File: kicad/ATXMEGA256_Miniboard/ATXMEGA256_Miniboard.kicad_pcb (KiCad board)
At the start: 4 copper layers, 50 x 70 mm, 42 parts, among them J1 1x2 Screw Terminal, J10 2x5 Goldpin Socket, J11 2x5 Goldpin Socket, J12 2x3 Goldpin Socket, J13 2x5 Goldpin Socket, J14 2x5 Goldpin Socket, J2 10118192-0001LF, J3 2x5 IDC Socket, J4 2x3 Goldpin Socket, J5 2x3 Goldpin Header, J6 1x2 Goldpin Header, J7 1x2 Goldpin Header, J8 1x3 Goldpin Header, J9 2x5 Goldpin Socket, Q1 MMFTP3334K, SW1 RESET, U1 ATXMEGA256A3B-AU, U2 MCP1703A-3302E/DB, Y1 32.768 kHz, Y2 16 MHz

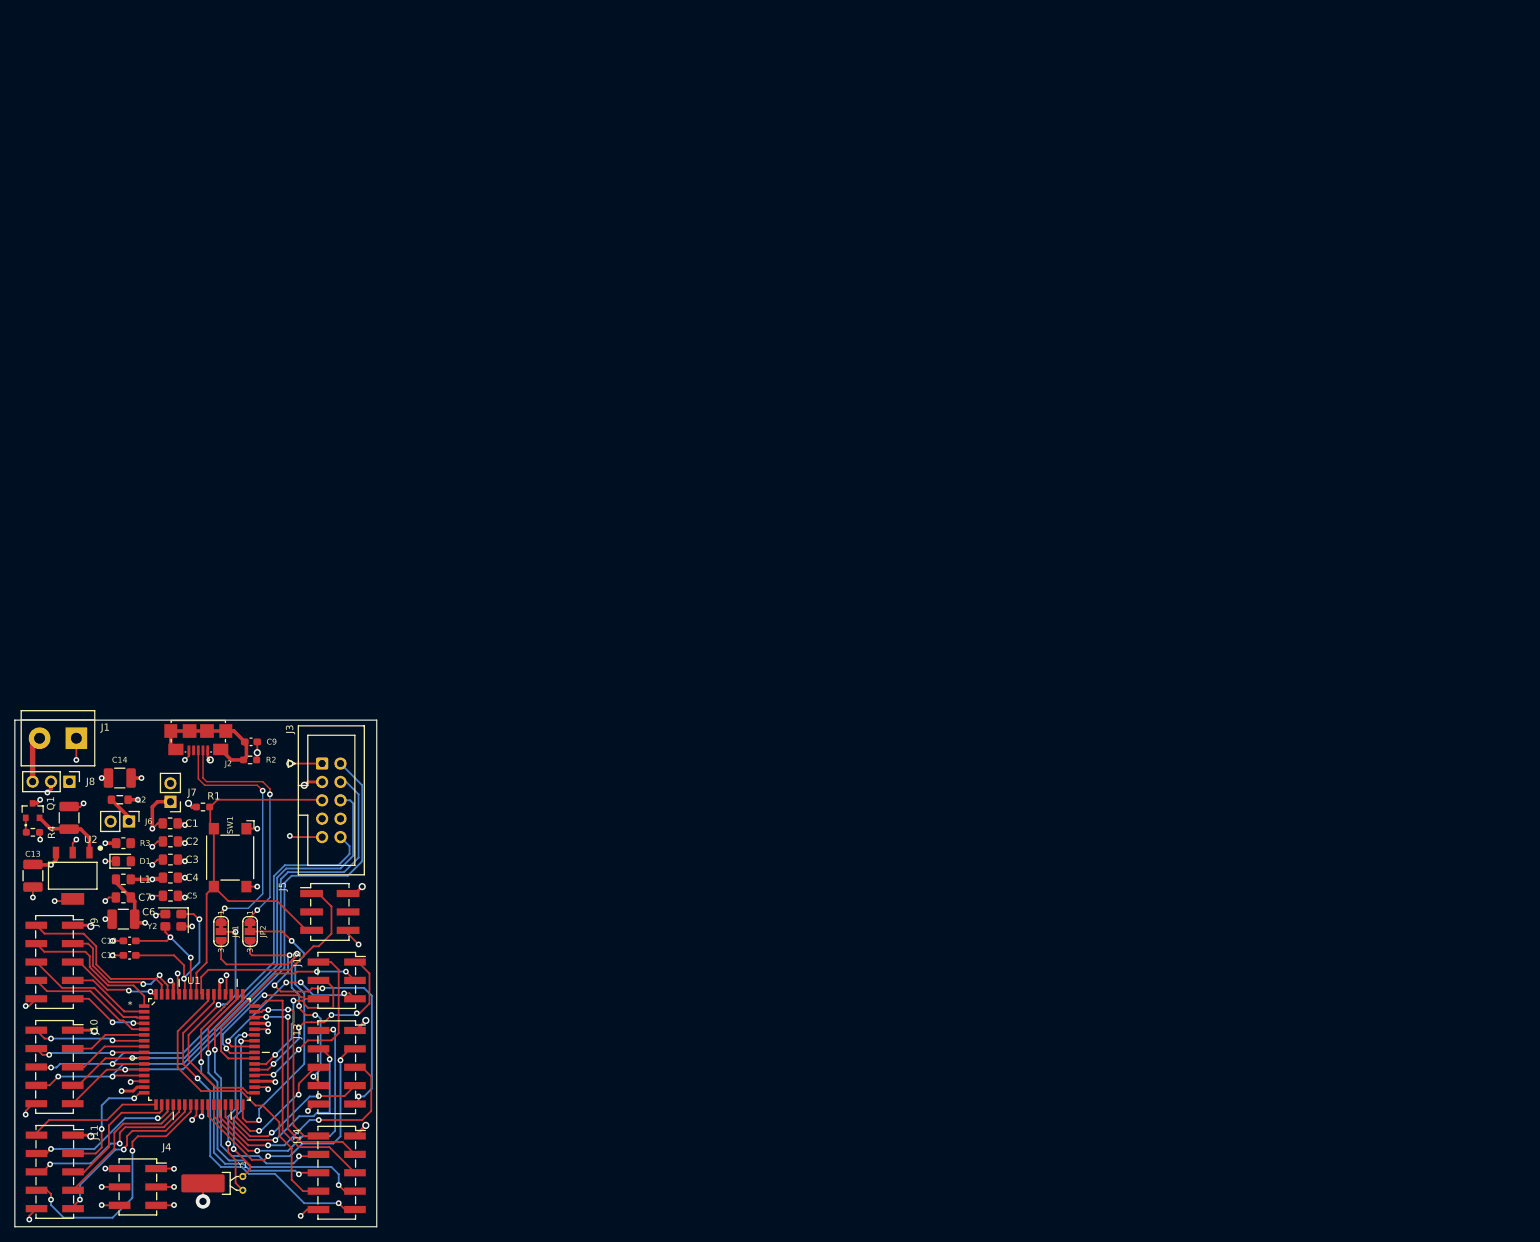
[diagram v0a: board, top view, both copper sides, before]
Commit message: layout komponentów
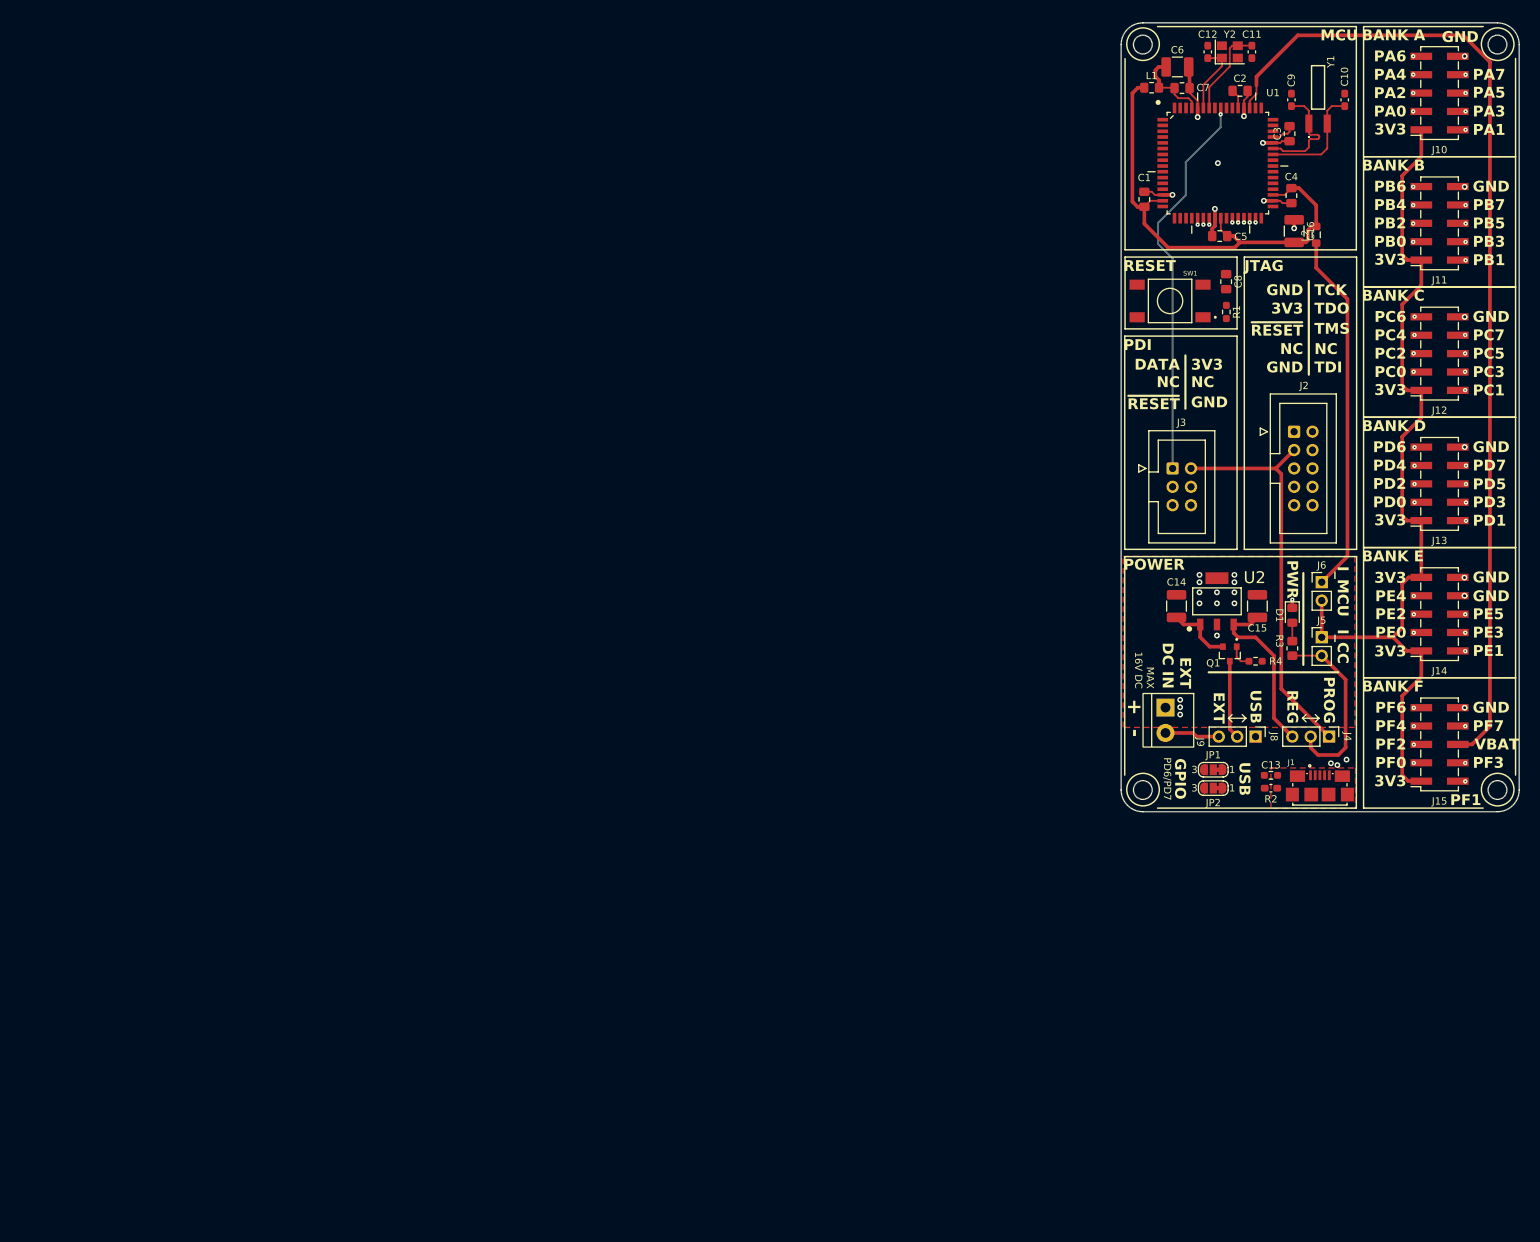
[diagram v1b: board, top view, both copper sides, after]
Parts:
- removed J7: 1x2 Goldpin Header, Connector_PinHeader_2.54mm:PinHeader_1x02_P2.54mm_Vertical
- added C15: 10u, Capacitor_SMD:C_1210_3225Metric_Pad1.33x2.70mm_HandSolder, F.Cu at (186.7, 110.7)
- added C16: 10u, Capacitor_SMD:C_1210_3225Metric_Pad1.33x2.70mm_HandSolder, F.Cu at (191.8, 58.9)
- added C8: 100n, Capacitor_SMD:C_0805_2012Metric_Pad1.18x1.45mm_HandSolder, F.Cu at (182.4, 65.9)
- added G***: LOGO, logo:onyx_logo, B.Cu at (316.2, 90.7)
- added J15: 2x5 Goldpin Socket, Connector_PinSocket_2.54mm:PinSocket_2x05_P2.54mm_Vertical_SMD, F.Cu at (211.9, 129.9)
- added REF**: KiCad-Logo2_6mm_SilkScreen, Symbol:KiCad-Logo2_6mm_SilkScreen, B.Cu at (350.3, 92.8)
- added REF**: ESD-Logo_6.6x6mm_SilkScreen, Symbol:ESD-Logo_6.6x6mm_SilkScreen, B.Cu at (334.0, 120.8)
- added REF**: OSHW-Logo2_14.6x12mm_SilkScreen, Symbol:OSHW-Logo2_14.6x12mm_SilkScreen, B.Cu at (375.4, 90.0)
- C10: value 12p -> 22p
- C12: value 10u -> 12p; footprint Capacitor_SMD:C_1210_3225Metric_Pad1.33x2.70mm_HandSolder -> Capacitor_SMD:C_0603_1608Metric_Pad1.08x0.95mm_HandSolder
- C13: value 10u -> 4n7; footprint Capacitor_SMD:C_1210_3225Metric_Pad1.33x2.70mm_HandSolder -> Capacitor_SMD:C_0603_1608Metric_Pad1.08x0.95mm_HandSolder
- C9: value 4n7 -> 22p
- J1: value 1x2 Screw Terminal -> 10118192-0001LF; footprint TerminalBlock:TerminalBlock_bornier-2_P5.08mm -> 10118192-0001LF:AMPHENOL_10118192-0001LF
- J12: value 2x3 Goldpin Socket -> 2x5 Goldpin Socket; footprint Connector_PinSocket_2.54mm:PinSocket_2x03_P2.54mm_Vertical_SMD -> Connector_PinSocket_2.54mm:PinSocket_2x05_P2.54mm_Vertical_SMD
- J2: value 10118192-0001LF -> 2x5 IDC Socket; footprint 10118192-0001LF:AMPHENOL_10118192-0001LF -> Connector_IDC:IDC-Header_2x05_P2.54mm_Vertical
- J3: value 2x5 IDC Socket -> 2x3 IDC Socket; footprint Connector_IDC:IDC-Header_2x05_P2.54mm_Vertical -> Connector_IDC:IDC-Header_2x03_P2.54mm_Vertical
- J4: value 2x3 Goldpin Socket -> 1x3 Goldpin Header; footprint Connector_PinSocket_2.54mm:PinSocket_2x03_P2.54mm_Vertical_SMD -> Connector_PinHeader_2.54mm:PinHeader_1x03_P2.54mm_Vertical
- J5: value 2x3 Goldpin Header -> 1x2 Goldpin Header; footprint Connector_PinHeader_2.54mm:PinHeader_2x03_P2.54mm_Vertical_SMD -> Connector_PinHeader_2.54mm:PinHeader_1x02_P2.54mm_Vertical
- J9: value 2x5 Goldpin Socket -> 1x2 Screw Terminal; footprint Connector_PinSocket_2.54mm:PinSocket_2x05_P2.54mm_Vertical_SMD -> DG381-3.5-02P-13-00AH:DG381-3.5-02P-13-00AH
- SW1: footprint Button_Switch_SMD:SW_SPST_Omron_B3FS-100xP -> FSM2JSMAA:SW_SMD_2-1437565-8_4_4.50_6.00_6.00_5.00
- Y1: footprint Crystal:Crystal_DS26_D2.0mm_L6.0mm_Horizontal_1EP_style1 -> LFXTAL025159:LFXTAL025159Reel
- moved J10 234.0 mm to (211.9, 39.9), turned to 180 degrees
- moved J11 231.9 mm to (211.9, 57.9), turned to 180 degrees
- moved Y1 211.5 mm to (195.1, 39.1)
- moved C10 204.2 mm to (198.8, 40.8), turned to -90 degrees
- moved C11 199.1 mm to (185.9, 34.2), turned to 90 degrees
- moved C12 189.6 mm to (179.8, 34.2)
- moved Y2 189.0 mm to (182.9, 34.2), turned to 0 degrees
- moved C6 187.3 mm to (175.6, 36.2), turned to 180 degrees
- moved U1 186.6 mm to (181.2, 49.5)
- moved C3 184.3 mm to (191.1, 45.5), turned to 90 degrees
- moved C7 184.1 mm to (176.3, 39.2), turned to 180 degrees
- moved L2 182.8 mm to (194.8, 59.4), turned to 90 degrees
- moved C4 181.3 mm to (191.4, 54.0), turned to 90 degrees
- moved C2 180.6 mm to (184.3, 39.5)
- moved L1 179.3 mm to (172.1, 39.1), turned to 0 degrees
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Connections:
- C1 pad 2: /Power Supply/VCC_MCU -> +3V3_MCU
- C10 pad 2: Net-(U1-PR0) -> Net-(U1-TOSC2)
- C11 pad 2: Net-(U1-PR1) -> Net-(U1-PR0)
- C12 pad 2: Net-(U2-VIN) -> Net-(U1-PR1)
- C13 pad 2: +3V3 -> SHIELD
- C14 pad 2: Net-(J7-Pin_2) -> Net-(U2-VIN)
- C2 pad 2: /Power Supply/VCC_MCU -> +3V3_MCU
- C3 pad 2: /Power Supply/VCC_MCU -> +3V3_MCU
- C4 pad 2: /Power Supply/VCC_MCU -> +3V3_MCU
- C5 pad 2: /Power Supply/VCC_MCU -> +3V3_MCU
- C9 pad 2: Net-(J2-SHIELD) -> Net-(U1-TOSC1)
- J1 pad 1: GND -> +5V_USB
- J1 pad 2: /Power Supply/VCC_EXT -> /D-
- J10 pad 1: +3V3 -> +3V3_IO
- J10 pad 2: /PB1 -> /PA1
- J10 pad 3: /PB0 -> /PA0
- J10 pad 4: /PB3 -> /PA3
- J10 pad 5: /PB2 -> /PA2
- J10 pad 6: /PB5 -> /PA5
- J10 pad 7: /PB4 -> /PA4
- J10 pad 8: /PB7 -> /PA7
- J10 pad 9: /PB6 -> /PA6
- J11 pad 1: +3V3 -> +3V3_IO
- J11 pad 2: /PC1 -> /PB1
- J11 pad 3: /PC0 -> /PB0
- J11 pad 4: /PC3 -> /PB3
- J11 pad 5: /PC2 -> /PB2
- J11 pad 6: /PC5 -> /PB5
- J11 pad 7: /PC4 -> /PB4
- J11 pad 8: /PC7 -> /PB7
- J11 pad 9: /PC6 -> /PB6
- J12 pad 1: /PE1 -> +3V3_IO
- J12 pad 2: /PE0 -> /PC1
- J12 pad 3: /PE3 -> /PC0
- J12 pad 4: /PE2 -> /PC3
- J12 pad 5: /PE5 -> /PC2
- J12 pad 6: /PE4 -> /PC5
- J13 pad 1: +3V3 -> +3V3_IO
- J14 pad 1: +3V3 -> +3V3_IO
- J14 pad 2: /PF1 -> /PE1
- J14 pad 3: /PF0 -> /PE0
- J14 pad 4: /PF3 -> /PE3
- J14 pad 5: /PF2 -> /PE2
- J14 pad 6: /VBAT -> /PE5
- J14 pad 7: /PF4 -> /PE4
- J14 pad 8: /PF7 -> GND
- J14 pad 9: /PF6 -> +3V3_IO
- J2 pad 1: +5V -> GND
- J2 pad 2: /D- -> /PB6
- J2 pad 3: /D+ -> +3V3_EXT
- J2 pad 4: unconnected-(J2-ID-Pad4) -> /PB7
- J2 pad 5: GND -> /~{RESET}
- J2 pad 6: Net-(J2-SHIELD) -> /PB4
- J3 pad 1: GND -> /PDI_DATA
- J3 pad 2: /PB6 -> +3V3_EXT
- J3 pad 3: +3V3 -> unconnected-(J3-Pin_3-Pad3)
- J3 pad 4: /PB7 -> unconnected-(J3-Pin_4-Pad4)
- J3 pad 6: /PB4 -> GND
- J4 pad 1: GND -> +3V3_EXT
- J4 pad 2: GND -> Net-(J4-Pin_2)
- J4 pad 3: GND -> Net-(J4-Pin_3)
- J5 pad 1: /PDI_DATA -> +3V3_IO
- J5 pad 2: +3V3 -> Net-(J4-Pin_2)
- J6 pad 2: +3V3 -> +3V3_IO
- J8 pad 1: +5V -> +5V_USB
- J8 pad 3: /Power Supply/VCC_EXT -> Net-(J8-Pin_3)
- J9 pad 1: +3V3 -> GND
- J9 pad 2: /PA1 -> Net-(J8-Pin_3)
- L1 pad 1: /Power Supply/VCC_MCU -> +3V3_MCU
- L2 pad 2: Net-(J7-Pin_2) -> +3V3_MCU
- R1 pad 1: /Power Supply/VCC_MCU -> +3V3_MCU
- R2 pad 1: Net-(J2-SHIELD) -> GND
- R2 pad 2: GND -> SHIELD
- R3 pad 1: +3V3 -> Net-(J4-Pin_2)
- U1 pad 15: /Power Supply/VCC_MCU -> +3V3_MCU
- U1 pad 25: /Power Supply/VCC_MCU -> +3V3_MCU
- U1 pad 35: /Power Supply/VCC_MCU -> +3V3_MCU
- U1 pad 45: /Power Supply/VCC_MCU -> +3V3_MCU
- U1 pad 53: /Power Supply/VCC_MCU -> +3V3_MCU
- U2 pad 3: +3V3 -> Net-(J4-Pin_3)
- Y1 pad 1: Net-(U1-TOSC2) -> Net-(U1-TOSC1)
- Y1 pad 2: Net-(U1-TOSC1) -> Net-(U1-TOSC2)
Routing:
- net GND: track 439.4 -> 29.7 mm, vias 44 -> 33
- net +3V3: track 199.0 -> 0.00 mm, vias 9 -> 0
- net +3V3_IO: track 0.00 -> 123.7 mm
- net /Power Supply/VCC_MCU: track 117.2 -> 0.00 mm, vias 11 -> 0
- net /VBAT: track 40.1 -> 138.1 mm, vias 2 -> 0
- net /PB7: track 81.1 -> 0.00 mm, vias 2 -> 1
- net /PB6: track 78.2 -> 0.00 mm
- net +3V3_MCU: track 0.00 -> 72.6 mm
- net /PB4: track 69.8 -> 0.00 mm
- net /PB5: track 69.8 -> 0.00 mm, vias 2 -> 1
- net /~{RESET}: track 58.6 -> 0.00 mm
- net +3V3_EXT: track 0.00 -> 55.4 mm
- net /PF6: track 48.7 -> 0.00 mm, vias 2 -> 1
- net Net-(J6-Pin_1): track 4.00 -> 50.1 mm
- net /PF4: track 45.8 -> 0.00 mm, vias 2 -> 1
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- added copper zone on F.Cu, net GND
- added copper zone on In2.Cu, net GND
- added copper zone on F.Cu, net SHIELD
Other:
- board size 50 x 70 mm -> 55 x 109 mm
- board text added: "+"
- board text added: "-"
- board text added: "0"
- board text added: "0 mm"
- board text added: "0.01 mm"
- board text added: "0.02"
- board text added: "0.035 mm"
- board text added: "0.1 mm"
- board text added: "0.1000 mm / 0.1000 mm"
- board text added: "0.1500 mm"
- board text added: "1"
- board text added: "1.24 mm"
- board text added: "1.6000 mm"
- board text added: "3.3"
- board text added: "3V3"
- board text added: "4"
- board text added: "4.5"
- board text added: "89.2376 mm x 113.8915 mm"
- board text added: "ATXMEGA256 Miniboard"
- board text added: "B.Cu"
- board text added: "B.Mask"
- board text added: "B.Paste"
- board text added: "B.Silkscreen"
- board text added: "BANK A"
- board text added: "BANK B"
- board text added: "BANK C"
- board text added: "BANK D"
- board text added: "BANK E"
- board text added: "BANK F"
- board text added: "BOARD CHARACTERISTICS"
- board text added: "Black"
- board text added: "Board Thickness:"
- board text added: "Board overall dimensions:"
- board text added: "Bottom Silk Screen"
- board text added: "Bottom Solder Mask"
- board text added: "Bottom Solder Paste"
- board text added: "Castellated pads:"
- board text added: "Color"
- board text added: "Copper Finish:"
- board text added: "Copper Layer Count:"
- board text added: "DATA"
- board text added: "Dielectric 1"
- board text added: "Dielectric 2"
- board text added: "Dielectric 3"
- board text added: "EXT"
- board text added: "EXT DC IN"
- board text added: "Edge card connectors:"
- board text added: "Epsilon R"
- board text added: "F.Cu"
- board text added: "F.Mask"
- board text added: "F.Paste"
- board text added: "F.Silkscreen"
- board text added: "FR4"
- board text added: "FR4 natural"
- board text added: "GND"
- board text added: "GPIO"
- board text added: "HAL lead-free"
- board text added: "I_CC"
- board text added: "I_MCU"
- board text added: "Impedance Control:"
- board text added: "In1.Cu"
- board text added: "In2.Cu"
- board text added: "JTAG"
- board text added: "Koło Naukowe Mikrosystemów ONYKS"
- board text added: "Layer Name"
- board text added: "Loss Tangent"
- board text added: "MAX 16V DC"
- board text added: "MCU"
- board text added: "Material"
- board text added: "Min hole diameter:"
- board text added: "Min track/spacing:"
- board text added: "NC"
- board text added: "No"
- board text added: "Not specified"
- board text added: "PA0"
- board text added: "PA1"
- board text added: "PA2"
- board text added: "PA3"
- board text added: "PA4"
- board text added: "PA5"
- board text added: "PA6"
- board text added: "PA7"
- board text added: "PB0"
- board text added: "PB1"
- board text added: "PB2"
- board text added: "PB3"
- board text added: "PB4"
- board text added: "PB5"
- board text added: "PB6"
- board text added: "PB7"
- board text added: "PC0"
- board text added: "PC1"
- board text added: "PC2"
- board text added: "PC3"
- board text added: "PC4"
- board text added: "PC5"
- board text added: "PC6"
- board text added: "PC7"
- board text added: "PD0"
- board text added: "PD1"
- board text added: "PD2"
- board text added: "PD3"
- board text added: "PD4"
- board text added: "PD5"
- board text added: "PD6"
- board text added: "PD6/PD7"
- board text added: "PD7"
- board text added: "PDI"
- board text added: "PE0"
- board text added: "PE1"
- board text added: "PE2"
- board text added: "PE3"
- board text added: "PE4"
- board text added: "PE5"
- board text added: "PF0"
- board text added: "PF1"
- board text added: "PF2"
- board text added: "PF3"
- board text added: "PF4"
- board text added: "PF6"
- board text added: "PF7"
- board text added: "POWER"
- board text added: "PROG"
- board text added: "PWR"
- board text added: "Plated Board Edge:"
- board text added: "REG"
- board text added: "RESET"
- board text added: "Rev. 1.3 2025"
- board text added: "Szymon Bartosik Mateusz Turycz Marcin Krawiec"
- board text added: "TCK"
- board text added: "TDI"
- board text added: "TDO"
- board text added: "TMS"
- board text added: "Thickness (mm)"
- board text added: "Top Silk Screen"
- board text added: "Top Solder Mask"
- board text added: "Top Solder Paste"
- board text added: "Type"
- board text added: "USB"
- board text added: "VBAT"
- board text added: "White"
- board text added: "copper"
- board text added: "core"
- board text added: "prepreg"
- board text added: "~{RESET}"

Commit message: wstepne poczenia
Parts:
- REF**: moved to F.Cu
- moved REF** 154.0 mm to (180.6, 134.6)
- moved G*** 122.1 mm to (195.5, 72.9)
- moved JP2 86.4 mm to (162.3, 51.4), turned to -90 degrees
- moved JP1 84.5 mm to (159.8, 51.4), turned to -90 degrees
- moved C9 46.2 mm to (194.5, 86.9), turned to 0 degrees
- moved C10 46.1 mm to (198.4, 86.9), turned to 180 degrees
- moved J3 42.8 mm to (177.2, 49.0)
- moved L2 42.5 mm to (197.2, 101.8), turned to 180 degrees
- moved C3 41.5 mm to (191.1, 87.0)
- moved C11 41.4 mm to (186.9, 75.6)
- moved C12 41.4 mm to (180.8, 75.6)
- moved Y2 41.4 mm to (183.9, 75.6)
- moved C2 41.4 mm to (183.7, 80.9)
- moved C4 41.4 mm to (191.3, 95.4)
- moved C7 41.4 mm to (176.2, 80.6)
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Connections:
- net Net-(U1-AVCC) renamed /MCU_AVCC
- SW1 pad 2: /~{RESET} -> GND
- SW1 pad 3: (no net) -> /~{RESET}
- SW1 pad 4: (no net) -> /~{RESET}
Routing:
- net /PA7: track 0.00 -> 101.5 mm, vias 1 -> 2
- net /PB6: track 0.00 -> 98.8 mm, vias 1 -> 2
- net /PB5: track 0.00 -> 98.5 mm, vias 1 -> 3
- net /PF1: track 0.00 -> 98.1 mm, vias 1 -> 2
- net /PB7: track 0.00 -> 97.5 mm, vias 1 -> 3
- net /PA5: track 0.00 -> 96.8 mm, vias 1 -> 2
- net /PF3: track 0.00 -> 96.4 mm, vias 1 -> 2
- net /PF6: track 0.00 -> 94.8 mm, vias 1 -> 2
- net /PF7: track 0.00 -> 93.9 mm, vias 1 -> 2
- net /PB4: track 0.00 -> 93.9 mm, vias 1 -> 2
- net /PA3: track 0.00 -> 91.4 mm, vias 1 -> 2
- net /PF0: track 0.00 -> 90.8 mm, vias 1 -> 2
- net /PA1: track 0.00 -> 90.6 mm, vias 1 -> 2
- net /PF4: track 0.00 -> 90.6 mm, vias 1 -> 2
- net /PA6: track 0.00 -> 90.4 mm, vias 1 -> 2
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- added copper zone on F.Cu, net /MCU_AVCC

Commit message: layout rev 0.9, zegar do poprawy
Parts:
- moved JP2 56.8 mm to (197.5, 96.0), turned to 90 degrees
- moved JP1 56.8 mm to (194.9, 96.0), turned to 90 degrees
- moved C8 9.80 mm to (177.7, 73.2), turned to 90 degrees
- moved L2 9.12 mm to (189.2, 106.3), turned to 90 degrees
- moved R1 7.91 mm to (175.6, 72.9), turned to 90 degrees
- moved J10 7.48 mm to (211.9, 47.3)
- moved C14 6.44 mm to (177.9, 116.7), turned to 0 degrees
- moved J11 5.83 mm to (211.9, 63.7)
- moved J12 4.33 mm to (211.9, 80.2)
- moved J3 3.12 mm to (177.3, 52.1)
- moved J13 2.83 mm to (211.9, 96.7)
- moved C11 2.81 mm to (184.4, 76.8), turned to 0 degrees
- moved C15 2.54 mm to (186.7, 113.3)
- moved SW1 2.47 mm to (177.5, 67.8)
- moved Y2 1.76 mm to (182.6, 74.3)
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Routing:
- net /PC0: track 0.00 -> 108.7 mm, vias 2 -> 4
- net /PC1: track 0.00 -> 100.2 mm, vias 2 -> 4
- net /PC2: track 0.00 -> 99.8 mm, vias 1 -> 4
- net /PC4: track 0.00 -> 97.7 mm, vias 1 -> 4
- net /PC3: track 0.00 -> 92.1 mm, vias 2 -> 4
- net /PC5: track 0.00 -> 90.0 mm, vias 2 -> 4
- net /PC6: track 0.00 -> 87.9 mm, vias 2 -> 4
- net /D-: track 0.00 -> 85.9 mm, vias 0 -> 2
- net /D+: track 0.00 -> 79.7 mm, vias 0 -> 2
- net /PC7: track 0.00 -> 79.2 mm, vias 2 -> 4
- net /PE1: track 8.22 -> 56.2 mm, vias 2 -> 4
- net /~{RESET}: track 26.1 -> 70.5 mm
- net /PE0: track 6.11 -> 49.1 mm, vias 2 -> 4
- net /PD1: track 0.00 -> 39.1 mm
- net /PD3: track 0.00 -> 37.2 mm
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- added copper zone on F.Cu, net +5V_USB
- added copper zone on F.Cu, net Net-(J4-Pin_3)
- added copper zone on F.Cu, net Net-(U2-VIN)
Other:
- board size 55 x 109 mm -> 55 x 102 mm
